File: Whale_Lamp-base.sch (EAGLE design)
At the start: 91 parts, among them Q2 20mA/30V, Q3 16MHz, Q5 2.5A/30V/105mΩ, U0 32U4

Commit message: finished board layout
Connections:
- removed net 3.3V: CORTEX_SWD1.SWDCLK/TCK
- net 5V: now also CORTEX_SWD1.SWDCLK/TCK
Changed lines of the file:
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@@
 <?xml version="1.0" encoding="utf-8"?>
 <!DOCTYPE eagle SYSTEM "eagle.dtd">
-<eagle version="9.6.2">
+<eagle version="8.3.1">
 <drawing>
 <settings>
@@
 <part name="R_LED" library="adafruit" deviceset="R-US_" device="R0402" value="510"/>
 <part name="U0" library="SparkFun-IC-Microcontroller" deviceset="ATMEGA32U4" device="QFN" value="32U4"/>
-<part name="SUPPLY7" library="SparkFun-PowerSymbols" deviceset="3.3V" device=""/>
 <part name="C_UCAP" library="adafruit" deviceset="C-US" device="C0603" value="2.2uF"/>
 <part name="C3" library="adafruit" deviceset="C-US" device="C0402" value="0.1uF"/>
@@
 <attribute name="VALUE" x="-27.94" y="55.88" size="1.778" layer="96"/>
 </instance>
-<instance part="SUPPLY7" gate="G$1" x="154.94" y="121.92" smashed="yes">
-<attribute name="VALUE" x="154.94" y="124.714" size="1.778" layer="96" align="bottom-center"/>
-</instance>
 <instance part="C_UCAP" gate="G$1" x="-43.18" y="104.14" smashed="yes">
 <attribute name="NAME" x="-42.164" y="104.775" size="1.778" layer="95"/>
@@
 <junction x="-38.1" y="81.28"/>
 <pinref part="U0" gate="G$1" pin="XTAL2"/>
-</segment>
-</net>
-<net name="3.3V" class="0">
-<segment>
-<pinref part="CORTEX_SWD1" gate="G$1" pin="SWDCLK/TCK"/>
-<wire x1="142.24" y1="119.38" x2="154.94" y2="119.38" width="0.1524" layer="91"/>
-<wire x1="154.94" y1="121.92" x2="154.94" y2="119.38" width="0.1524" layer="91"/>
-<pinref part="SUPPLY7" gate="G$1" pin="3.3V"/>
 </segment>
 </net>
@@
 <label x="-43.18" y="12.7" size="1.778" layer="95" rot="R90" xref="yes"/>
 </segment>
-</net>
+<segment>
+<pinref part="CORTEX_SWD1" gate="G$1" pin="SWDCLK/TCK"/>
+<wire x1="142.24" y1="119.38" x2="147.32" y2="119.38" width="0.1524" layer="91"/>
+<label x="147.32" y="119.38" size="1.27" layer="95" xref="yes"/>
+</segment>
+</net>

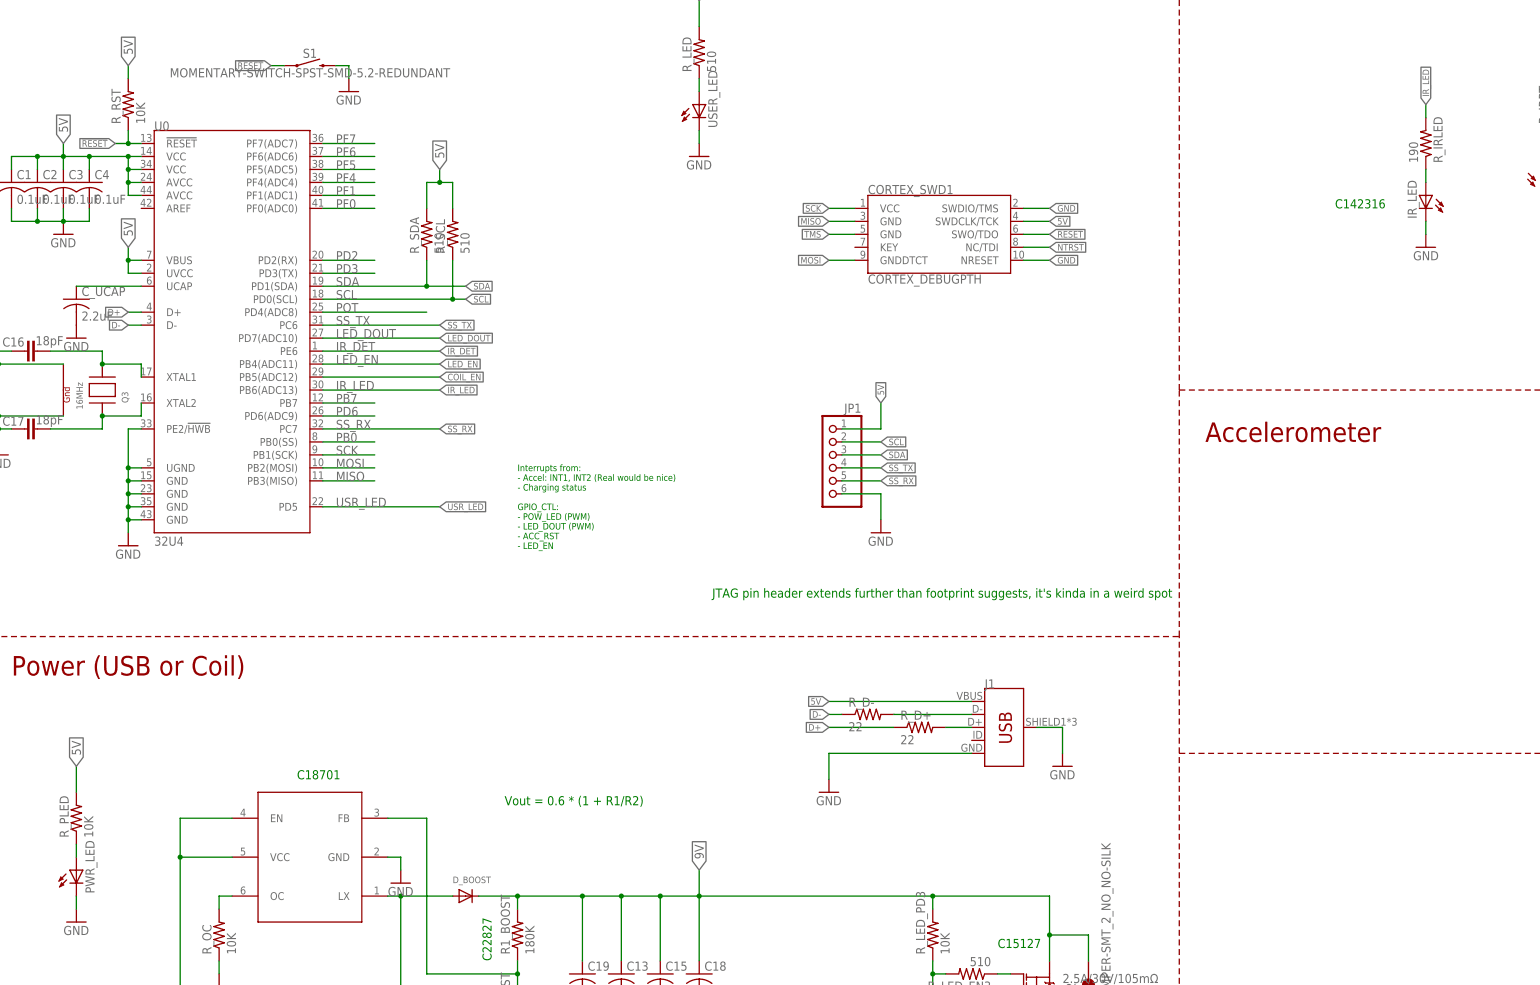
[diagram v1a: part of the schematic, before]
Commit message: Silkscreen cleanup and added additional info into schematic
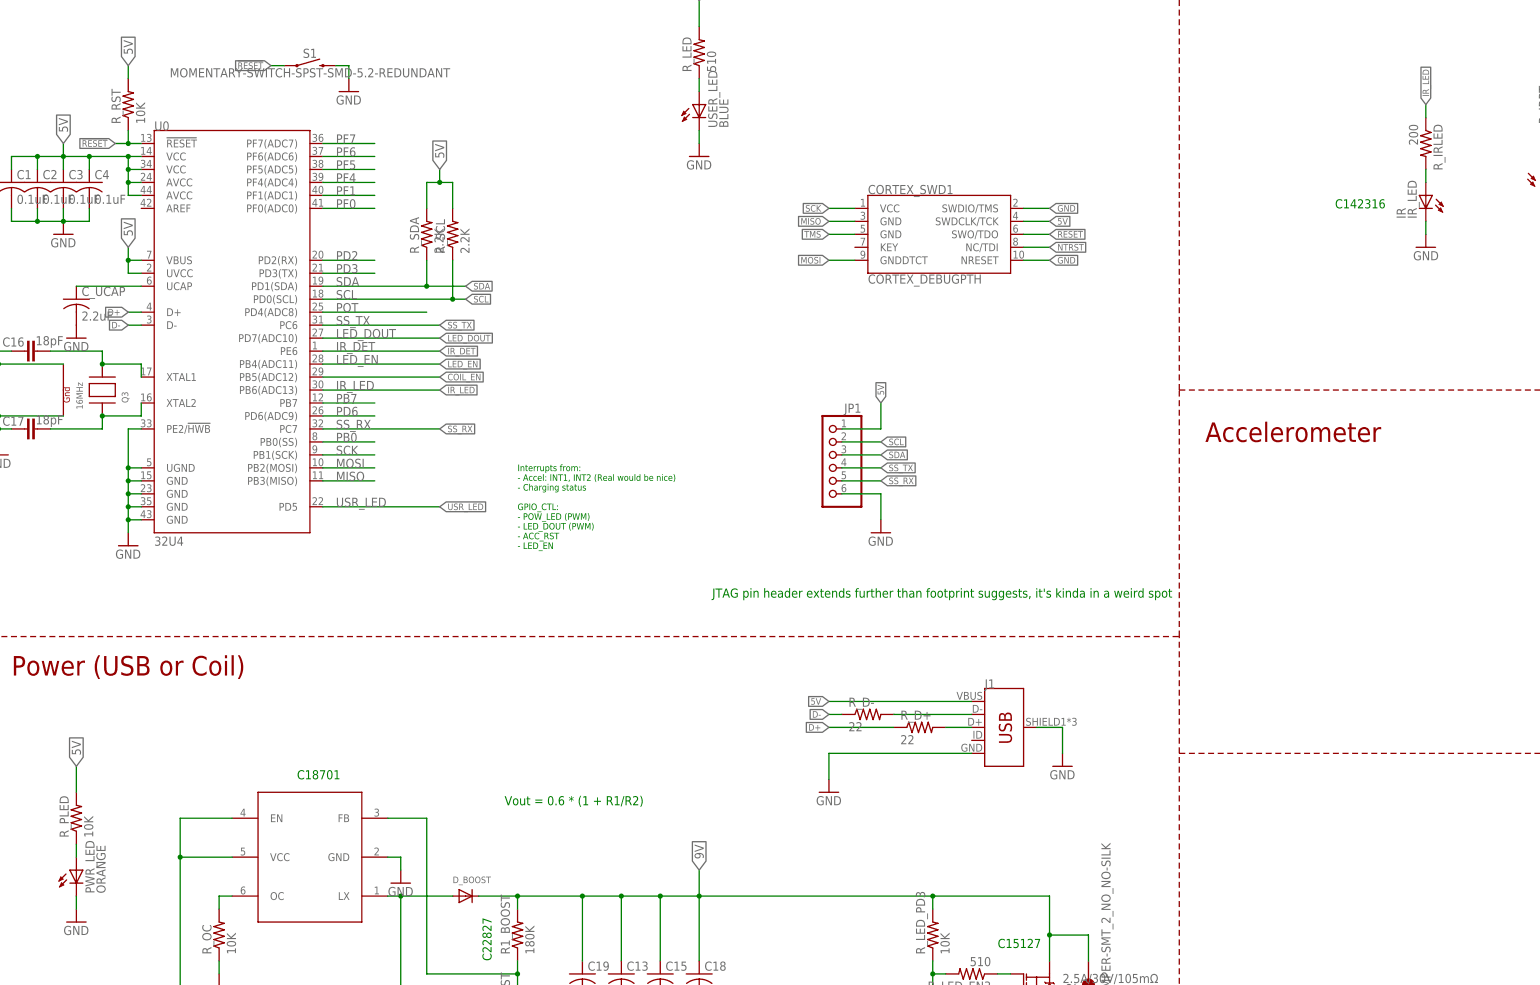
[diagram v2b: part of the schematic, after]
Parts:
- IR_LED: value (none) -> IR
- PWR_LED: value (none) -> ORANGE
- R_IRLED: value 190 -> 200; device adafruit:R-US_R0402 -> adafruit:R-US_R0603
- R_SCL, R_SDA: value 510 -> 2.2K
- USER_LED: value (none) -> BLUE
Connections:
- net IR_LED: now also R_IRLED.1; no longer R_IRLED.2
- net N$48: now also R_IRLED.2; no longer R_IRLED.1
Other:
- moved on the sheet: R_IRLED
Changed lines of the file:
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@@
 <parts>
 <part name="GND15" library="SparkFun-Aesthetics" deviceset="GND" device=""/>
-<part name="USER_LED" library="adafruit" deviceset="LED" device="CHIPLED_0603"/>
+<part name="USER_LED" library="adafruit" deviceset="LED" device="CHIPLED_0603" value="BLUE"/>
 <part name="GND12" library="SparkFun-Aesthetics" deviceset="GND" device=""/>
 <part name="FRAME1" library="frames" library_urn="urn:adsk.eagle:library:229" deviceset="DINA3_L" device=""/>
@@
 <part name="LED35" library="adafruit" library_urn="urn:adsk.eagle:library:420" deviceset="WS2812B" device="_5050N" package3d_urn="urn:adsk.eagle:package:6240961/1"/>
 <part name="LED36" library="adafruit" library_urn="urn:adsk.eagle:library:420" deviceset="WS2812B" device="_5050N" package3d_urn="urn:adsk.eagle:package:6240961/1"/>
-<part name="R_SDA" library="adafruit" deviceset="R-US_" device="R0402" value="510"/>
-<part name="R_SCL" library="adafruit" deviceset="R-US_" device="R0402" value="510"/>
+<part name="R_SDA" library="adafruit" deviceset="R-US_" device="R0402" value="2.2K"/>
+<part name="R_SCL" library="adafruit" deviceset="R-US_" device="R0402" value="2.2K"/>
 <part name="JP1" library="pinhead" library_urn="urn:adsk.eagle:library:325" deviceset="PINHD-1X6" device="" package3d_urn="urn:adsk.eagle:package:22472/2"/>
 <part name="GND1" library="SparkFun-Aesthetics" deviceset="GND" device=""/>
 <part name="S1" library="SparkFun-Switches" library_urn="urn:adsk.eagle:library:535" deviceset="MOMENTARY-SWITCH-SPST" device="-SMD-5.2-REDUNDANT" package3d_urn="urn:adsk.eagle:package:40167/1"/>
-<part name="PWR_LED" library="adafruit" deviceset="LED" device="CHIPLED_0603"/>
+<part name="PWR_LED" library="adafruit" deviceset="LED" device="CHIPLED_0603" value="ORANGE"/>
 <part name="GND31" library="SparkFun-Aesthetics" deviceset="GND" device=""/>
 <part name="R_PLED" library="adafruit" deviceset="R-US_" device="R0402" value="10K"/>
@@
 <part name="R_IRPT" library="adafruit" deviceset="R-US_" device="R0402" value="10K"/>
 <part name="GND3" library="SparkFun-Aesthetics" deviceset="GND" device=""/>
-<part name="IR_LED" library="adafruit" deviceset="LED" device="CHIPLED_0603"/>
+<part name="IR_LED" library="adafruit" deviceset="LED" device="CHIPLED_0603" value="IR"/>
 <part name="GND5" library="SparkFun-Aesthetics" deviceset="GND" device=""/>
-<part name="R_IRLED" library="adafruit" deviceset="R-US_" device="R0402" value="190"/>
 <part name="JP2" library="SparkFun-Jumpers" deviceset="JUMPER-SMT_2_NO" device="_NO-SILK"/>
 <part name="JST-COIL_IN1" library="adafruit" deviceset="JST_2PIN" device="-THM-RA"/>
@@
 <part name="J1" library="SparkFun-Connectors" deviceset="USB_MICRO-B" device="_FEMALE-SMT"/>
 <part name="GND16" library="SparkFun-Aesthetics" deviceset="GND" device=""/>
+<part name="R_IRLED" library="adafruit" deviceset="R-US_" device="R0603" value="200"/>
 </parts>
 <sheets>
@@
 <attribute name="VALUE" x="223.52" y="111.76" size="1.778" layer="96" rot="MR0"/>
 </instance>
-<instance part="R_IRLED" gate="G$1" x="220.98" y="134.62" smashed="yes" rot="MR90">
-<attribute name="NAME" x="222.4786" y="130.81" size="1.778" layer="95" rot="MR90"/>
-<attribute name="VALUE" x="217.678" y="130.81" size="1.778" layer="96" rot="MR90"/>
-</instance>
 <instance part="JP2" gate="G$1" x="154.94" y="-30.48" smashed="yes" rot="R90">
 <attribute name="NAME" x="152.4" y="-33.02" size="1.778" layer="95" font="vector" rot="R90"/>
@@
 <attribute name="VALUE" x="147.32" y="10.16" size="1.778" layer="96"/>
 </instance>
+<instance part="R_IRLED" gate="G$1" x="220.98" y="134.62" rot="R270"/>
 </instances>
 <busses>
@@
 <pinref part="IR_LED" gate="G$1" pin="A"/>
 <wire x1="220.98" y1="129.54" x2="220.98" y2="127" width="0.1524" layer="91"/>
-<pinref part="R_IRLED" gate="G$1" pin="1"/>
+<pinref part="R_IRLED" gate="G$1" pin="2"/>
 </segment>
 </net>
@@
 <wire x1="220.98" y1="139.7" x2="220.98" y2="142.24" width="0.1524" layer="91"/>
 <label x="220.98" y="142.24" size="1.27" layer="95" rot="MR90" xref="yes"/>
-<pinref part="R_IRLED" gate="G$1" pin="2"/>
-</segment>
-<segment>
+<pinref part="R_IRLED" gate="G$1" pin="1"/>
+</segment>
+<segment>
